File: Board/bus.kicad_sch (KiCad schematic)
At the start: 4 parts, among them IC16 74LVC8T245SO24, P4 CSABUS, U2 SN74LVC245APW, U3 SN74LVC245APW

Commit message: update
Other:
- note removed: "3.3V Generation for I/O"
- moved on the sheet: IC16, P4, U2, U3

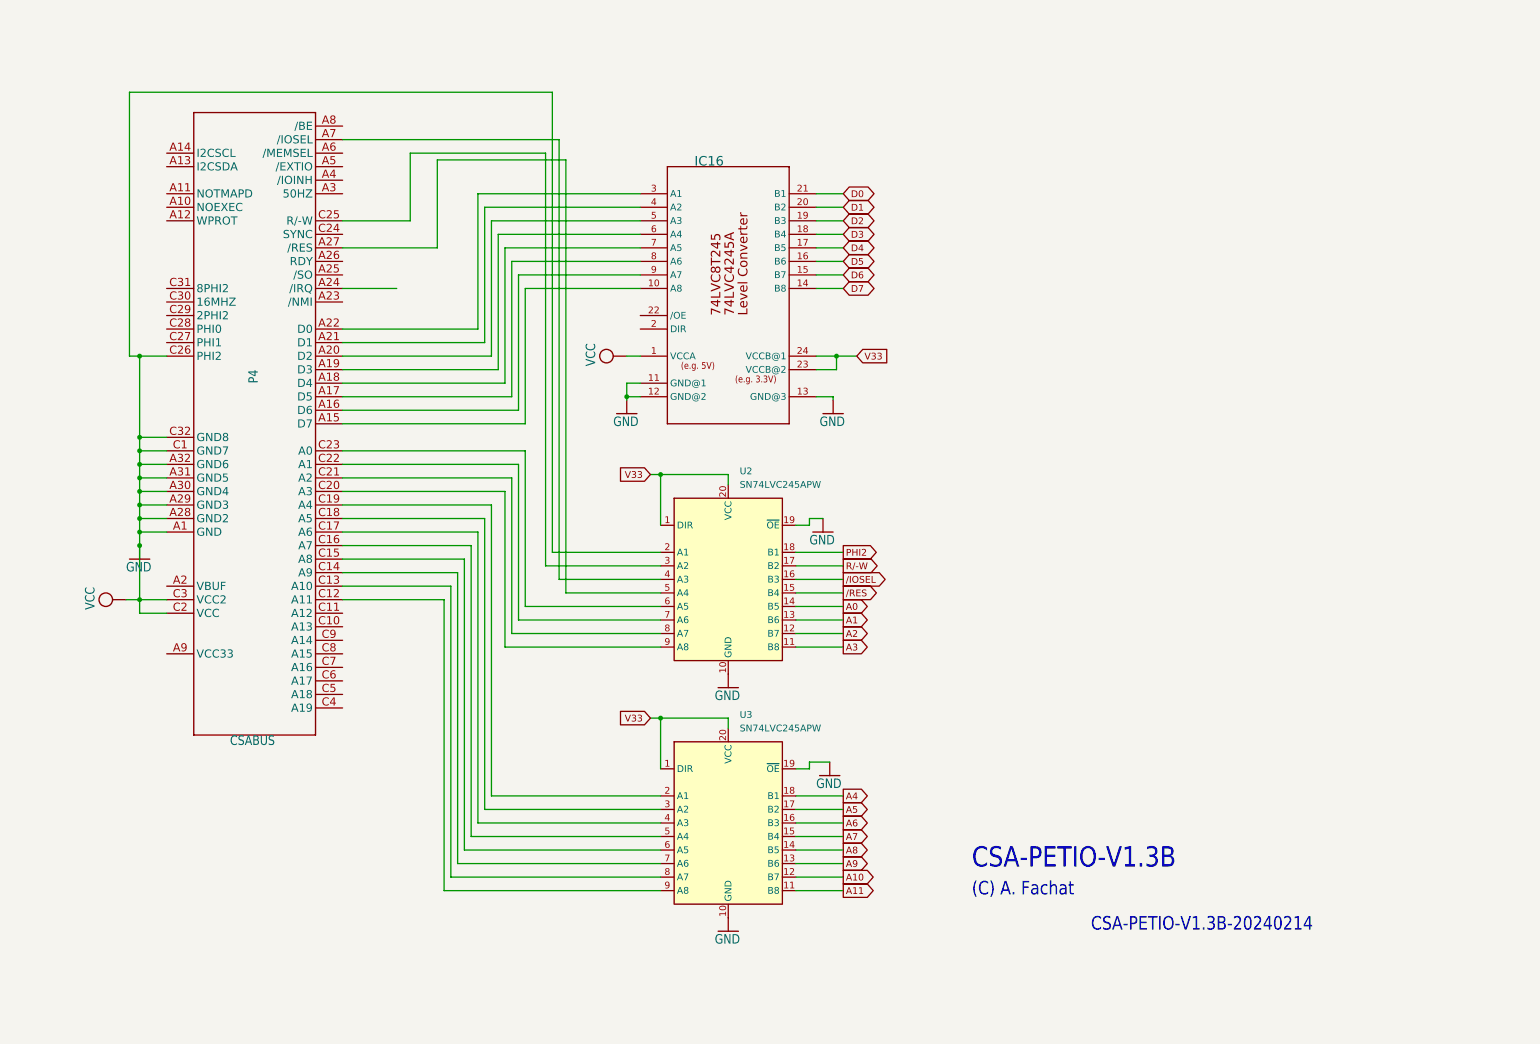
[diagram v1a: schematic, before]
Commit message: adding keyboard, serial IEC
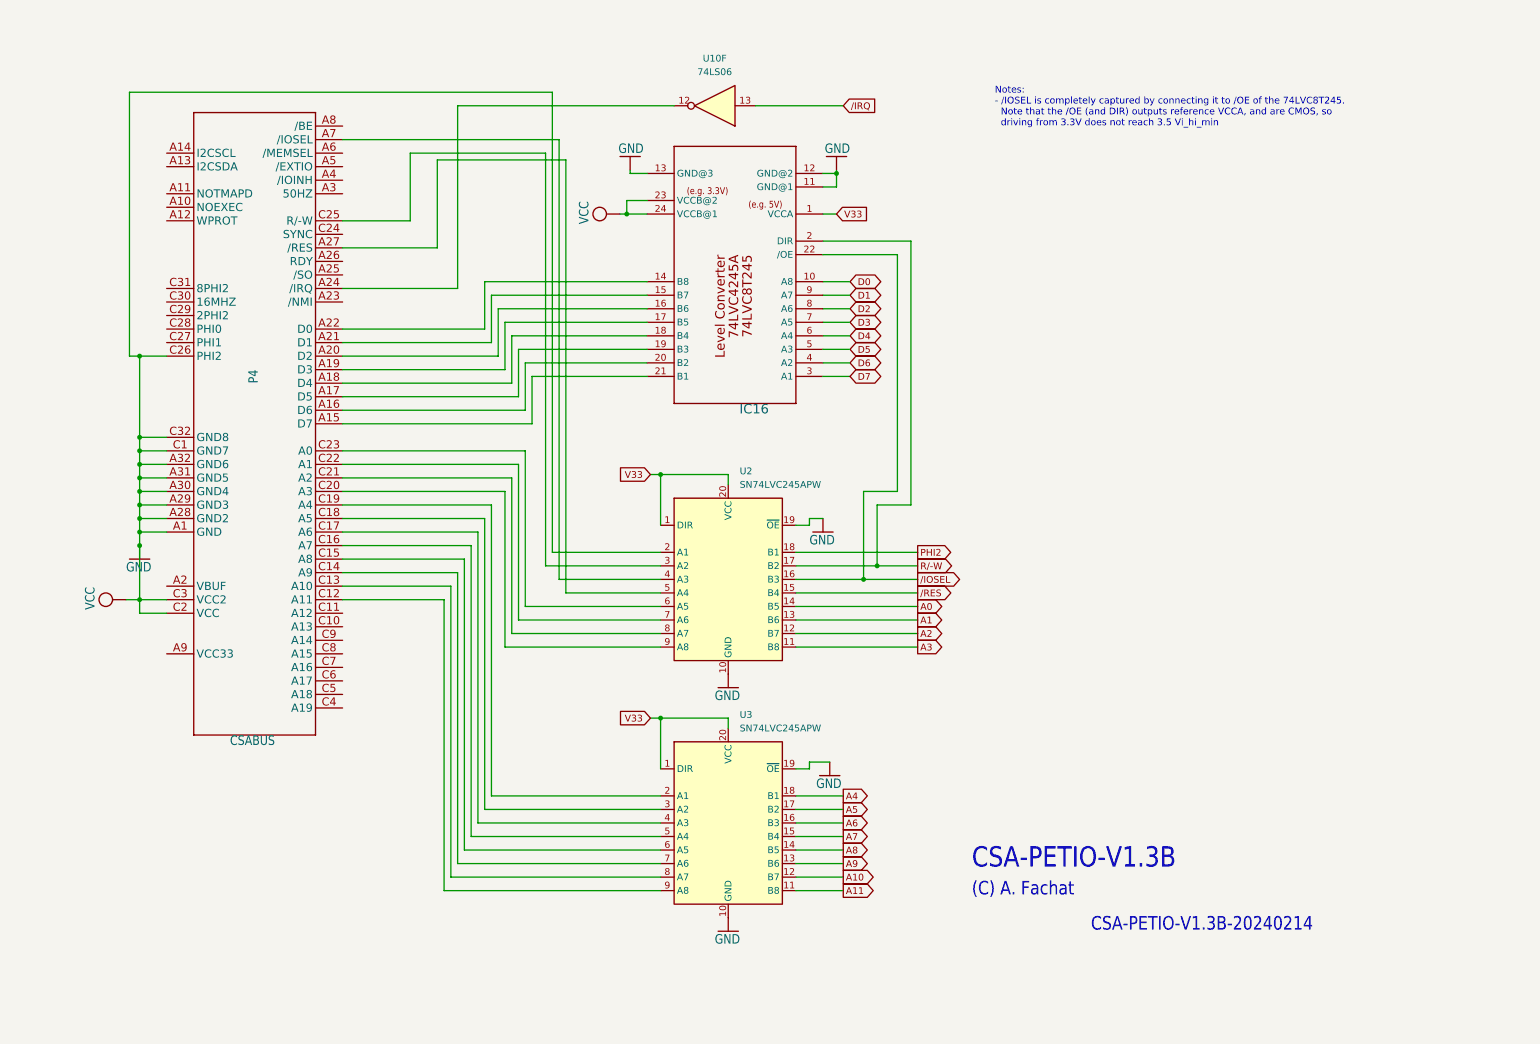
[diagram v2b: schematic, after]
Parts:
- added U10: 74LS06, Package_SO:SO-14_3.9x8.65mm_P1.27mm, symbol 74xx:74LS06
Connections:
- net D0: now also IC16.10 (A8); no longer IC16.21 (B1)
- net D1: now also IC16.9 (A7); no longer IC16.20 (B2)
- net D2: now also IC16.8 (A6); no longer IC16.19 (B3)
- net D3: now also IC16.7 (A5); no longer IC16.18 (B4)
- net D4: now also IC16.6 (A4); no longer IC16.17 (B5)
- net D5: now also IC16.5 (A3); no longer IC16.16 (B6)
- net D6: now also IC16.4 (A2); no longer IC16.15 (B7)
- net D7: now also IC16.3 (A1); no longer IC16.14 (B8)
- net GND: now also IC16.23 (VCCB@2), IC16.24 (VCCB@1); no longer IC16.1 (VCCA)
- net R/-W: now also IC16.2 (DIR)
- net V33: now also IC16.1 (VCCA); no longer IC16.23 (VCCB@2), IC16.24 (VCCB@1)
- net /IOSEL: now also IC16.22 (/OE)
- net at P4.A15 (D7): now also IC16.21 (B1); no longer IC16.10 (A8)
- net at P4.A16 (D6): now also IC16.20 (B2); no longer IC16.9 (A7)
- net at P4.A17 (D5): now also IC16.19 (B3); no longer IC16.8 (A6)
- net at P4.A18 (D4): now also IC16.18 (B4); no longer IC16.7 (A5)
- net at P4.A19 (D3): now also IC16.17 (B5); no longer IC16.6 (A4)
- net at P4.A20 (D2): now also IC16.16 (B6); no longer IC16.5 (A3)
- net at P4.A21 (D1): now also IC16.15 (B7); no longer IC16.4 (A2)
- net at P4.A22 (D0): now also IC16.14 (B8); no longer IC16.3 (A1)
- net at P4.A24 (/IRQ): now also U10.12
- new net /IRQ: U10.13
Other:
- note added: "Notes: - /IOSEL is completely captured by connecting it to /OE of the 74LVC8T245. Note that the /OE (and DIR) outputs reference VCCA, and are CMOS, so driving from 3.3V does not reach 3.5 Vi_hi_min"
- moved on the sheet: IC16

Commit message: add serial, SPI-10-5V
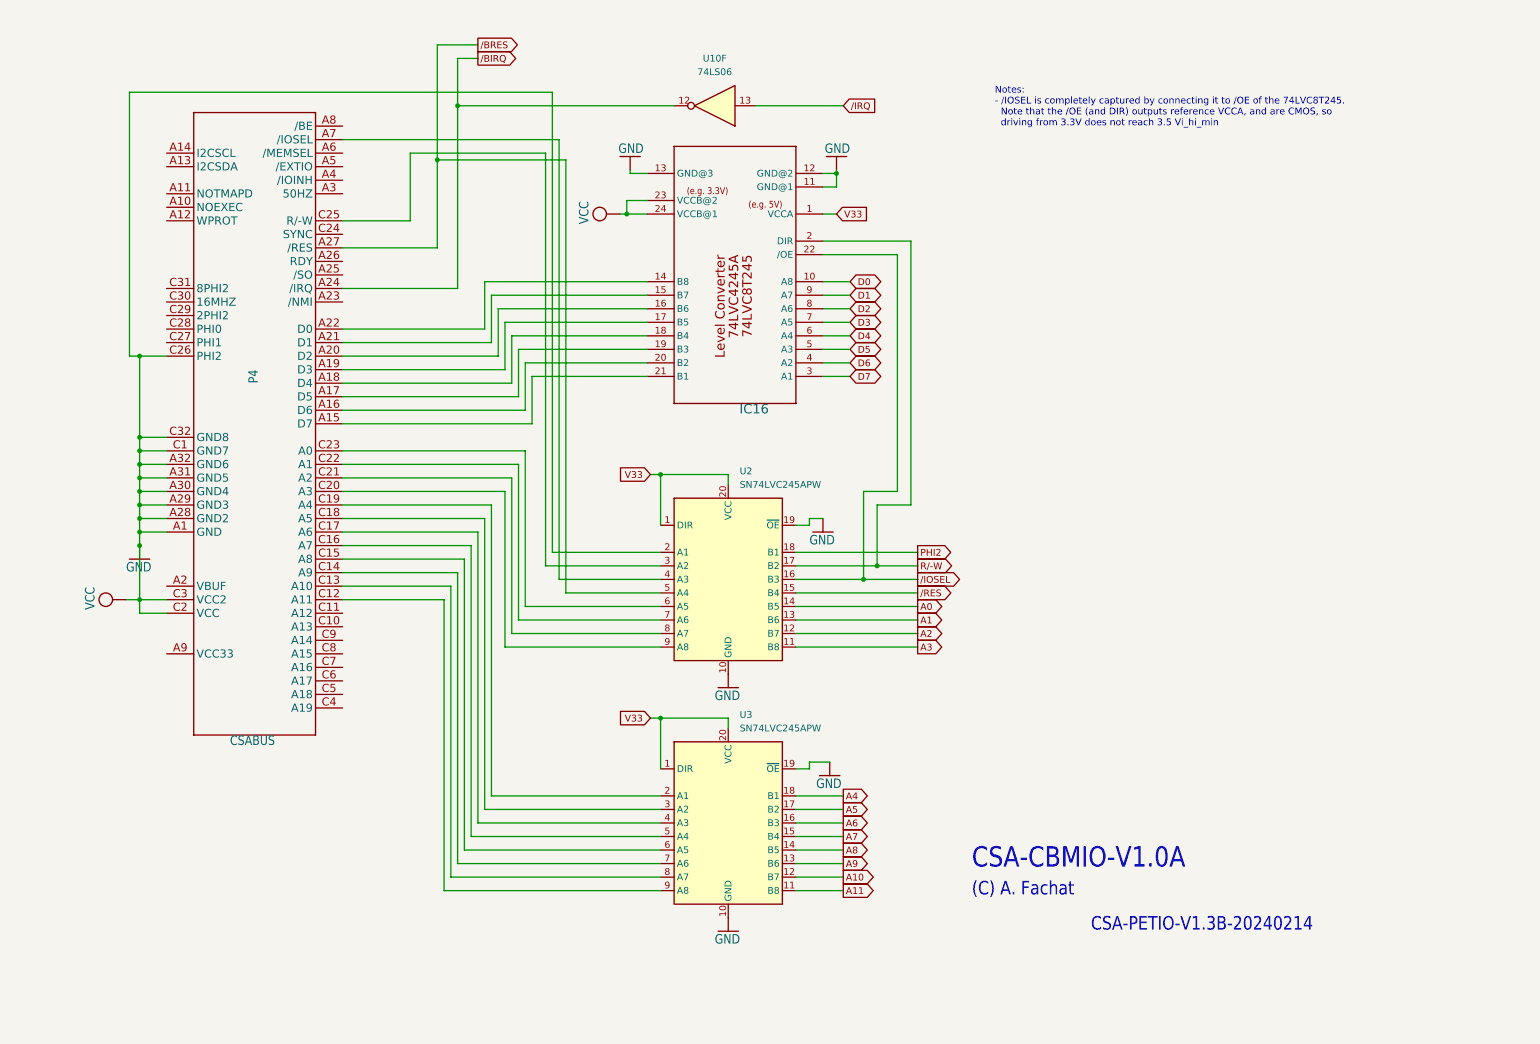
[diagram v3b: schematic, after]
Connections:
- net /BIRQ: now reaches P4.A24 (/IRQ), U10.12
- net /BRES: now reaches P4.A27 (/RES), U2.5 (A4)
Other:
- note added: "CSA-CBMIO-V1.0A"
- note removed: "CSA-PETIO-V1.3B"
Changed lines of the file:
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@@
 		)
 	)
-	(text "CSA-PETIO-V1.3B"
+	(text "CSA-CBMIO-V1.0A"
 		(exclude_from_sim no)
 		(at 186.69 173.99 0)
@@
 	)
 	(junction
+		(at 86.36 40.64)
+		(diameter 0)
+		(color 0 0 0 0)
+	)
+	(junction
 		(at 30.48 123.19)
 		(diameter 0)
@@
 		(color 0 0 0 0)
 	)
+	(junction
+		(at 90.17 30.48)
+		(diameter 0)
+		(color 0 0 0 0)
+	)
 	(wire
 		(pts
@@
 	(wire
 		(pts
+			(xy 93.98 19.05) (xy 86.36 19.05)
+		)
+		(stroke
+			(width 0)
+			(type default)
+		)
+	)
+	(wire
+		(pts
 			(xy 30.48 77.47) (xy 30.48 92.71)
 		)
@@
 	(wire
 		(pts
+			(xy 93.98 21.59) (xy 90.17 21.59)
+		)
+		(stroke
+			(width 0)
+			(type default)
+		)
+	)
+	(wire
+		(pts
 			(xy 106.68 39.37) (xy 106.68 116.84)
 		)
@@
 	(wire
 		(pts
+			(xy 90.17 21.59) (xy 90.17 30.48)
+		)
+		(stroke
+			(width 0)
+			(type default)
+		)
+	)
+	(wire
+		(pts
 			(xy 153.67 162.56) (xy 162.56 162.56)
 		)
@@
 		(pts
 			(xy 110.49 121.92) (xy 128.27 121.92)
+		)
+		(stroke
+			(width 0)
+			(type default)
+		)
+	)
+	(wire
+		(pts
+			(xy 86.36 19.05) (xy 86.36 40.64)
 		)
 		(stroke
@@
 		)
 	)
+	(global_label "{slash}BRES"
+		(shape output)
+		(at 93.98 19.05 0)
+		(fields_autoplaced yes)
+		(effects
+			(font
+				(size 1.27 1.27)
+			)
+			(justify left)
+		)
+		(property "Intersheetrefs" "${INTERSHEET_REFS}"
+			(at 103.1942 19.05 0)
+			(effects
+				(font
+					(size 1.27 1.27)
+				)
+				(justify left)
+				(hide yes)
+			)
+		)
+	)
 	(global_label "V33"
 		(shape input)
@@
 			(effects
 				(font
+					(size 1.27 1.27)
+				)
+				(justify left)
+				(hide yes)
+			)
+		)
+	)
+	(global_label "{slash}BIRQ"
+		(shape output)
+		(at 93.98 21.59 0)
+		(fields_autoplaced yes)
+		(effects
+			(font
+				(size 1.27 1.27)
+			)
+			(justify left)
+		)
+		(property "Intersheetrefs" "${INTERSHEET_REFS}"
+			(at 102.771 21.59 0)
+			(effects
+				(font

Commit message: schematics 1st full rev
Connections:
- net /IOSEL: no longer IC16.22 (/OE)
- new net /BE: IC16.22 (/OE)
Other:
- note added: "CSA-CBMIO-V1.0A-20250815"
- note added: "Notes: - Note that the /OE (and DIR) outputs reference VCCA, and are CMOS, so driving from 3.3V does not reach 3.5 Vi_hi_min"
- note removed: "CSA-PETIO-V1.3B-20240214"
- note removed: "Notes: - /IOSEL is completely captured by connecting it to /OE of the 74LVC8T245. Note that the /OE (and DIR) outputs reference VCCA, and are CMOS, so driving from 3.3V does not reach 3.5 Vi_hi_min"
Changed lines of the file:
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@@
 	(generator_version "9.0")
 	(paper "A4")
-	(text "Notes:\n- /IOSEL is completely captured by connecting it to /OE of the 74LVC8T245.\n  Note that the /OE (and DIR) outputs reference VCCA, and are CMOS, so \n  driving from 3.3V does not reach 3.5 Vi_hi_min"
+	(text "Notes:\n- Note that the /OE (and DIR) outputs reference VCCA, and are CMOS, so \n  driving from 3.3V does not reach 3.5 Vi_hi_min"
 		(exclude_from_sim no)
 		(at 191.008 30.734 0)
@@
 		)
 	)
-	(text "CSA-PETIO-V1.3B-20240214"
+	(text "CSA-CBMIO-V1.0A-20250815"
 		(exclude_from_sim no)
 		(at 209.042 185.674 0)
@@
 	)
 	(junction
-		(at 166.37 119.38)
-		(diameter 0)
-		(color 0 0 0 0)
-	)
-	(junction
 		(at 30.48 77.47)
 		(diameter 0)
@@
 	(wire
 		(pts
-			(xy 166.37 119.38) (xy 176.53 119.38)
-		)
-		(stroke
-			(width 0)
-			(type default)
-		)
-	)
-	(wire
-		(pts
 			(xy 96.52 105.41) (xy 96.52 160.02)
 		)
@@
 	(wire
 		(pts
-			(xy 153.67 119.38) (xy 166.37 119.38)
+			(xy 153.67 119.38) (xy 176.53 119.38)
 		)
 		(stroke
@@
 	(wire
 		(pts
+			(xy 158.75 58.42) (xy 161.29 58.42)
+		)
+		(stroke
+			(width 0)
+			(type default)
+		)
+	)
+	(wire
+		(pts
 			(xy 156.21 107.95) (xy 158.75 107.95)
 		)
@@
 	(wire
 		(pts
-			(xy 172.72 102.87) (xy 166.37 102.87)
-		)
-		(stroke
-			(width 0)
-			(type default)
-		)
-	)
-	(wire
-		(pts
 			(xy 125.73 50.8) (xy 121.92 50.8)
 		)
@@
 	(wire
 		(pts
-			(xy 166.37 102.87) (xy 166.37 119.38)
-		)
-		(stroke
-			(width 0)
-			(type default)
-		)
-	)
-	(wire
-		(pts
 			(xy 109.22 119.38) (xy 128.27 119.38)
 		)
@@
 	(wire
 		(pts
-			(xy 158.75 58.42) (xy 172.72 58.42)
-		)
-		(stroke
-			(width 0)
-			(type default)
-		)
-	)
-	(wire
-		(pts
 			(xy 87.63 177.8) (xy 128.27 177.8)
 		)
@@
 			(width 0.1524)
 			(type solid)
-		)
-	)
-	(wire
-		(pts
-			(xy 172.72 58.42) (xy 172.72 102.87)
-		)
-		(stroke
-			(width 0)
-			(type default)
 		)
 	)
@@
 			(effects
 				(font
+					(size 1.27 1.27)
+				)
+				(justify left)
+				(hide yes)
+			)
+		)
+	)
+	(global_label "{slash}BE"
+		(shape input)
+		(at 161.29 58.42 0)
+		(fields_autoplaced yes)
+		(effects
+			(font
+				(size 1.27 1.27)
+			)
+			(justify left)
+		)
+		(property "Intersheetrefs" "${INTERSHEET_REFS}"
+			(at 168.0247 58.42 0)
+			(effects
+				(font

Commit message: full connect, starting on prod
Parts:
- IC16: footprint Package_SO:SO-24_5.3x15mm_P1.27mm -> Package_SO:TSSOP-24_6.1x7.8mm_P0.65mm
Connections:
- net GND: no longer IC16.23 (VCCB@2), IC16.24 (VCCB@1), P4.C2 (VCC), P4.C26 (PHI2), P4.C3 (VCC2), U2.2 (A1)
- new net: P4.C26 (PHI2), U2.2 (A1)
- new net VCC: IC16.23 (VCCB@2), IC16.24 (VCCB@1), P4.C2 (VCC), P4.C3 (VCC2)
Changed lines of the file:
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@@
-	)
-	(junction
-		(at 30.48 77.47)
-		(diameter 0)
-		(color 0 0 0 0)
 	)
 	(junction
@@
 	)
 	(junction
-		(at 30.48 92.71)
-		(diameter 0)
-		(color 0 0 0 0)
-	)
-	(junction
 		(at 30.48 97.79)
 		(diameter 0)
@@
 	)
 	(junction
-		(at 30.48 113.03)
-		(diameter 0)
-		(color 0 0 0 0)
-	)
-	(junction
 		(at 30.48 102.87)
 		(diameter 0)
@@
 	(wire
 		(pts
-			(xy 35.56 77.47) (xy 30.48 77.47)
-		)
-		(stroke
-			(width 0)
-			(type default)
-		)
-	)
-	(wire
-		(pts
 			(xy 153.67 132.08) (xy 176.53 132.08)
 		)
@@
 	(wire
 		(pts
-			(xy 30.48 123.19) (xy 30.48 113.03)
-		)
-		(stroke
-			(width 0.1524)
-			(type solid)
-		)
-	)
-	(wire
-		(pts
 			(xy 161.29 43.18) (xy 161.29 42.545)
 		)
@@
 	(wire
 		(pts
-			(xy 30.48 77.47) (xy 30.48 92.71)
-		)
-		(stroke
-			(width 0.1524)
-			(type solid)
-		)
-	)
-	(wire
-		(pts
 			(xy 68.58 113.03) (xy 92.71 113.03)
 		)
@@
 	(wire
 		(pts
-			(xy 30.48 77.47) (xy 28.575 77.47)
+			(xy 28.575 77.47) (xy 35.56 77.47)
 		)
 		(stroke
@@
 			)
 		)
-		(property "Footprint" "Package_SO:SO-24_5.3x15mm_P1.27mm"
+		(property "Footprint" "Package_SO:TSSOP-24_6.1x7.8mm_P0.65mm"
 			(at 146.05 63.5 0)
 			(effects

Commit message: 1st working as 1.0B
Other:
- note added: "CSA-CBMIO-V1.0B"
- note removed: "CSA-CBMIO-V1.0A"
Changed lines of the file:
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@@
 		)
 	)
-	(text "CSA-CBMIO-V1.0A"
+	(text "CSA-CBMIO-V1.0B"
 		(exclude_from_sim no)
 		(at 186.69 173.99 0)
